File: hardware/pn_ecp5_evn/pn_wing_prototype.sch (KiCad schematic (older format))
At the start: 23 parts, among them J101 Screw_Terminal_01x02, J102 Conn_Coaxial, J103 Conn_02x20_Odd_Even, J104 Conn_Coaxial, J105 Conn_Coaxial, J106 Conn_Coaxial, J107 Conn_01x10

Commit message: added part numbers to schematic of phase noise downconverter, ordered
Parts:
- H101, H102, H103, H104, H105, H106, H107, H108, H109, H110, H111, H112, H113, H114, H115, H116, J107: Distributor Part Number (none) -> N/A
- J101: Distributor (none) -> Digi-Key; Distributor Part Number (none) -> 277-1273-ND
- J102, J104, J105, J106: Distributor (none) -> Digi-Key; Distributor Part Number (none) -> WM5534-ND
- J103: Distributor (none) -> Digi-Key; Distributor Part Number (none) -> S7053-ND
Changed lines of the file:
@@
 F 2 "vna:SMA_Molex_73251-1153_OSHFR408" H 1150 1750 50  0001 C CNN
 F 3 " ~" H 1150 1750 50  0001 C CNN
+F 4 "WM5534-ND" H 1150 1750 50  0001 C CNN "Distributor Part Number"
+F 5 "Digi-Key" H 1150 1750 50  0001 C CNN "Distributor"
 	1    1150 1750
 	-1   0    0    -1
@@
 F 2 "vna:SMA_Molex_73251-1153_OSHFR408" H 9150 1650 50  0001 C CNN
 F 3 " ~" H 9150 1650 50  0001 C CNN
+F 4 "WM5534-ND" H 9150 1650 50  0001 C CNN "Distributor Part Number"
+F 5 "Digi-Key" H 9150 1650 50  0001 C CNN "Distributor"
 	1    9150 1650
 	1    0    0    -1
@@
 F 2 "vna:SMA_Molex_73251-1153_OSHFR408" H 9150 2150 50  0001 C CNN
 F 3 " ~" H 9150 2150 50  0001 C CNN
+F 4 "WM5534-ND" H 9150 2150 50  0001 C CNN "Distributor Part Number"
+F 5 "Digi-Key" H 9150 2150 50  0001 C CNN "Distributor"
 	1    9150 2150
 	1    0    0    -1
@@
 F 2 "vna:SMA_Molex_73251-1153_OSHFR408" H 9150 2700 50  0001 C CNN
 F 3 " ~" H 9150 2700 50  0001 C CNN
+F 4 "WM5534-ND" H 9150 2700 50  0001 C CNN "Distributor Part Number"
+F 5 "Digi-Key" H 9150 2700 50  0001 C CNN "Distributor"
 	1    9150 2700
 	1    0    0    -1
@@
 F 2 "Connector_PinSocket_2.54mm:PinSocket_2x20_P2.54mm_Vertical" H 9050 4850 50  0001 C CNN
 F 3 "~" H 9050 4850 50  0001 C CNN
+F 4 "Digi-Key" H 9050 4850 50  0001 C CNN "Distributor"
+F 5 "S7053-ND " H 9050 4850 50  0001 C CNN "Distributor Part Number"
 	1    9050 4850
 	1    0    0    -1
@@
 F 2 "Connector_PinHeader_2.54mm:PinHeader_1x10_P2.54mm_Vertical" H 10200 4350 50  0001 C CNN
 F 3 "~" H 10200 4350 50  0001 C CNN
+F 4 "N/A" H 10200 4350 50  0001 C CNN "Distributor Part Number"
 	1    10200 4350
 	1    0    0    -1
@@
 F 2 "TerminalBlock_Phoenix:TerminalBlock_Phoenix_MPT-0,5-2-2.54_1x02_P2.54mm_Horizontal" H 1000 5350 50  0001 C CNN
 F 3 "~" H 1000 5350 50  0001 C CNN
+F 4 "Digi-Key" H 1000 5350 50  0001 C CNN "Distributor"
+F 5 "277-1273-ND" H 1000 5350 50  0001 C CNN "Distributor Part Number"
 	1    1000 5350
 	-1   0    0    -1
@@
 F 2 "MountingHole:MountingHole_2.7mm_M2.5_ISO14580_Pad" H 1000 7450 50  0001 C CNN
 F 3 "~" H 1000 7450 50  0001 C CNN
+F 4 "N/A" H 1000 7450 50  0001 C CNN "Distributor Part Number"
 	1    1000 7450
 	1    0    0    -1
@@
 F 2 "MountingHole:MountingHole_2.7mm_M2.5_ISO14580_Pad" H 1300 7450 50  0001 C CNN
 F 3 "~" H 1300 7450 50  0001 C CNN
+F 4 "N/A" H 1300 7450 50  0001 C CNN "Distributor Part Number"
 	1    1300 7450
 	1    0    0    -1
@@
 F 2 "MountingHole:MountingHole_2.7mm_M2.5_ISO14580_Pad" H 1600 7450 50  0001 C CNN
 F 3 "~" H 1600 7450 50  0001 C CNN
+F 4 "N/A" H 1600 7450 50  0001 C CNN "Distributor Part Number"
 	1    1600 7450
 	1    0    0    -1
@@
 F 2 "MountingHole:MountingHole_2.7mm_M2.5_ISO14580_Pad" H 1900 7450 50  0001 C CNN
 F 3 "~" H 1900 7450 50  0001 C CNN
+F 4 "N/A" H 1900 7450 50  0001 C CNN "Distributor Part Number"
 	1    1900 7450
 	1    0    0    -1
@@
 F 2 "MountingHole:MountingHole_2.7mm_M2.5_ISO14580_Pad" H 2200 7450 50  0001 C CNN
 F 3 "~" H 2200 7450 50  0001 C CNN
+F 4 "N/A" H 2200 7450 50  0001 C CNN "Distributor Part Number"
 	1    2200 7450
 	1    0    0    -1
@@
 F 2 "MountingHole:MountingHole_2.7mm_M2.5_ISO14580_Pad" H 2500 7450 50  0001 C CNN
 F 3 "~" H 2500 7450 50  0001 C CNN
+F 4 "N/A" H 2500 7450 50  0001 C CNN "Distributor Part Number"
 	1    2500 7450
 	1    0    0    -1
@@
 F 2 "MountingHole:MountingHole_2.7mm_M2.5_ISO14580_Pad" H 2800 7450 50  0001 C CNN
 F 3 "~" H 2800 7450 50  0001 C CNN
+F 4 "N/A" H 2800 7450 50  0001 C CNN "Distributor Part Number"
 	1    2800 7450
 	1    0    0    -1
@@
 F 2 "MountingHole:MountingHole_2.7mm_M2.5_ISO14580_Pad" H 3100 7450 50  0001 C CNN
 F 3 "~" H 3100 7450 50  0001 C CNN
+F 4 "N/A" H 3100 7450 50  0001 C CNN "Distributor Part Number"
 	1    3100 7450
 	1    0    0    -1
@@
 F 2 "MountingHole:MountingHole_2.7mm_M2.5_ISO14580_Pad" H 3400 7450 50  0001 C CNN
 F 3 "~" H 3400 7450 50  0001 C CNN
+F 4 "N/A" H 3400 7450 50  0001 C CNN "Distributor Part Number"
 	1    3400 7450
 	1    0    0    -1
@@
 F 2 "MountingHole:MountingHole_2.7mm_M2.5_ISO14580_Pad" H 3700 7450 50  0001 C CNN
 F 3 "~" H 3700 7450 50  0001 C CNN
+F 4 "N/A" H 3700 7450 50  0001 C CNN "Distributor Part Number"
 	1    3700 7450
 	1    0    0    -1
@@
 F 2 "MountingHole:MountingHole_2.7mm_M2.5_ISO14580_Pad" H 4000 7450 50  0001 C CNN
 F 3 "~" H 4000 7450 50  0001 C CNN
+F 4 "N/A" H 4000 7450 50  0001 C CNN "Distributor Part Number"
 	1    4000 7450
 	1    0    0    -1
@@
 F 2 "MountingHole:MountingHole_2.7mm_M2.5_ISO14580_Pad" H 4300 7450 50  0001 C CNN
 F 3 "~" H 4300 7450 50  0001 C CNN
+F 4 "N/A" H 4300 7450 50  0001 C CNN "Distributor Part Number"
 	1    4300 7450
 	1    0    0    -1
@@
 F 2 "MountingHole:MountingHole_2.7mm_M2.5_ISO14580_Pad" H 4650 7450 50  0001 C CNN
 F 3 "~" H 4650 7450 50  0001 C CNN
+F 4 "N/A" H 4650 7450 50  0001 C CNN "Distributor Part Number"
 	1    4650 7450
 	1    0    0    -1
@@
 F 2 "MountingHole:MountingHole_2.7mm_M2.5_ISO14580_Pad" H 4950 7450 50  0001 C CNN
 F 3 "~" H 4950 7450 50  0001 C CNN
+F 4 "N/A" H 4950 7450 50  0001 C CNN "Distributor Part Number"
 	1    4950 7450
 	1    0    0    -1
@@
 F 2 "MountingHole:MountingHole_2.7mm_M2.5_ISO14580_Pad" H 5400 7450 50  0001 C CNN
 F 3 "~" H 5400 7450 50  0001 C CNN
+F 4 "N/A" H 5400 7450 50  0001 C CNN "Distributor Part Number"
 	1    5400 7450
 	1    0    0    -1
@@
 F 2 "MountingHole:MountingHole_2.7mm_M2.5_ISO14580_Pad" H 5800 7450 50  0001 C CNN
 F 3 "~" H 5800 7450 50  0001 C CNN
+F 4 "N/A" H 5800 7450 50  0001 C CNN "Distributor Part Number"
 	1    5800 7450
 	1    0    0    -1

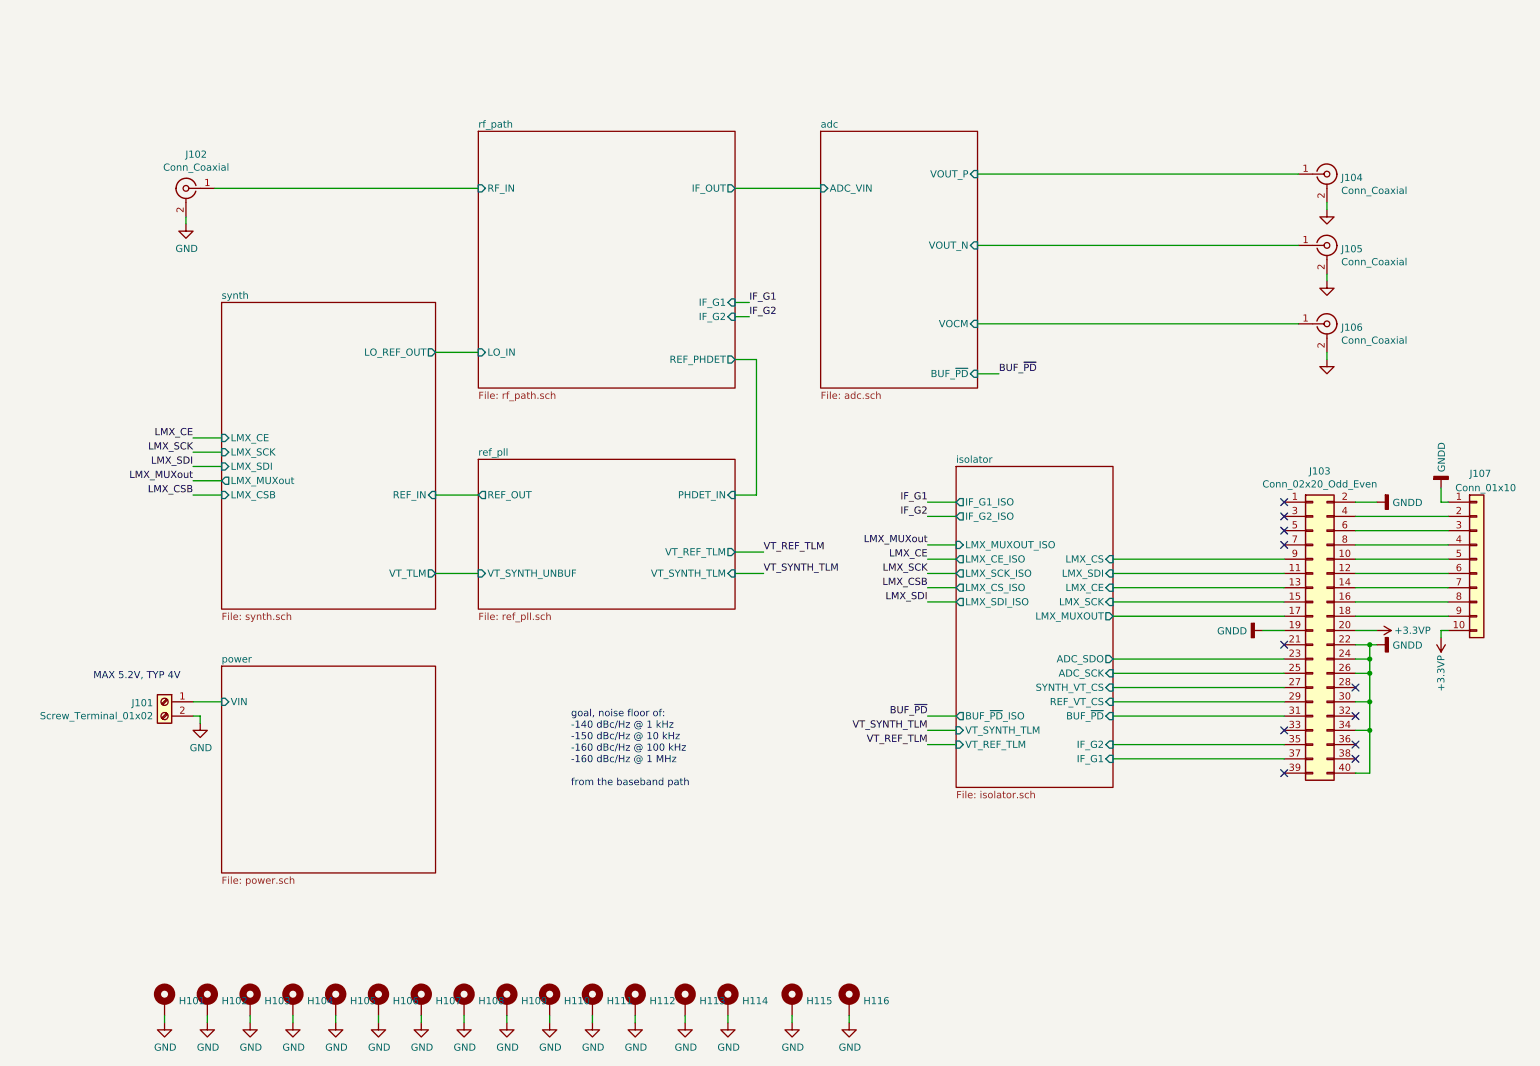
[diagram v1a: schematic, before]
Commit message: added schematic export, updated README, schematic cleanup
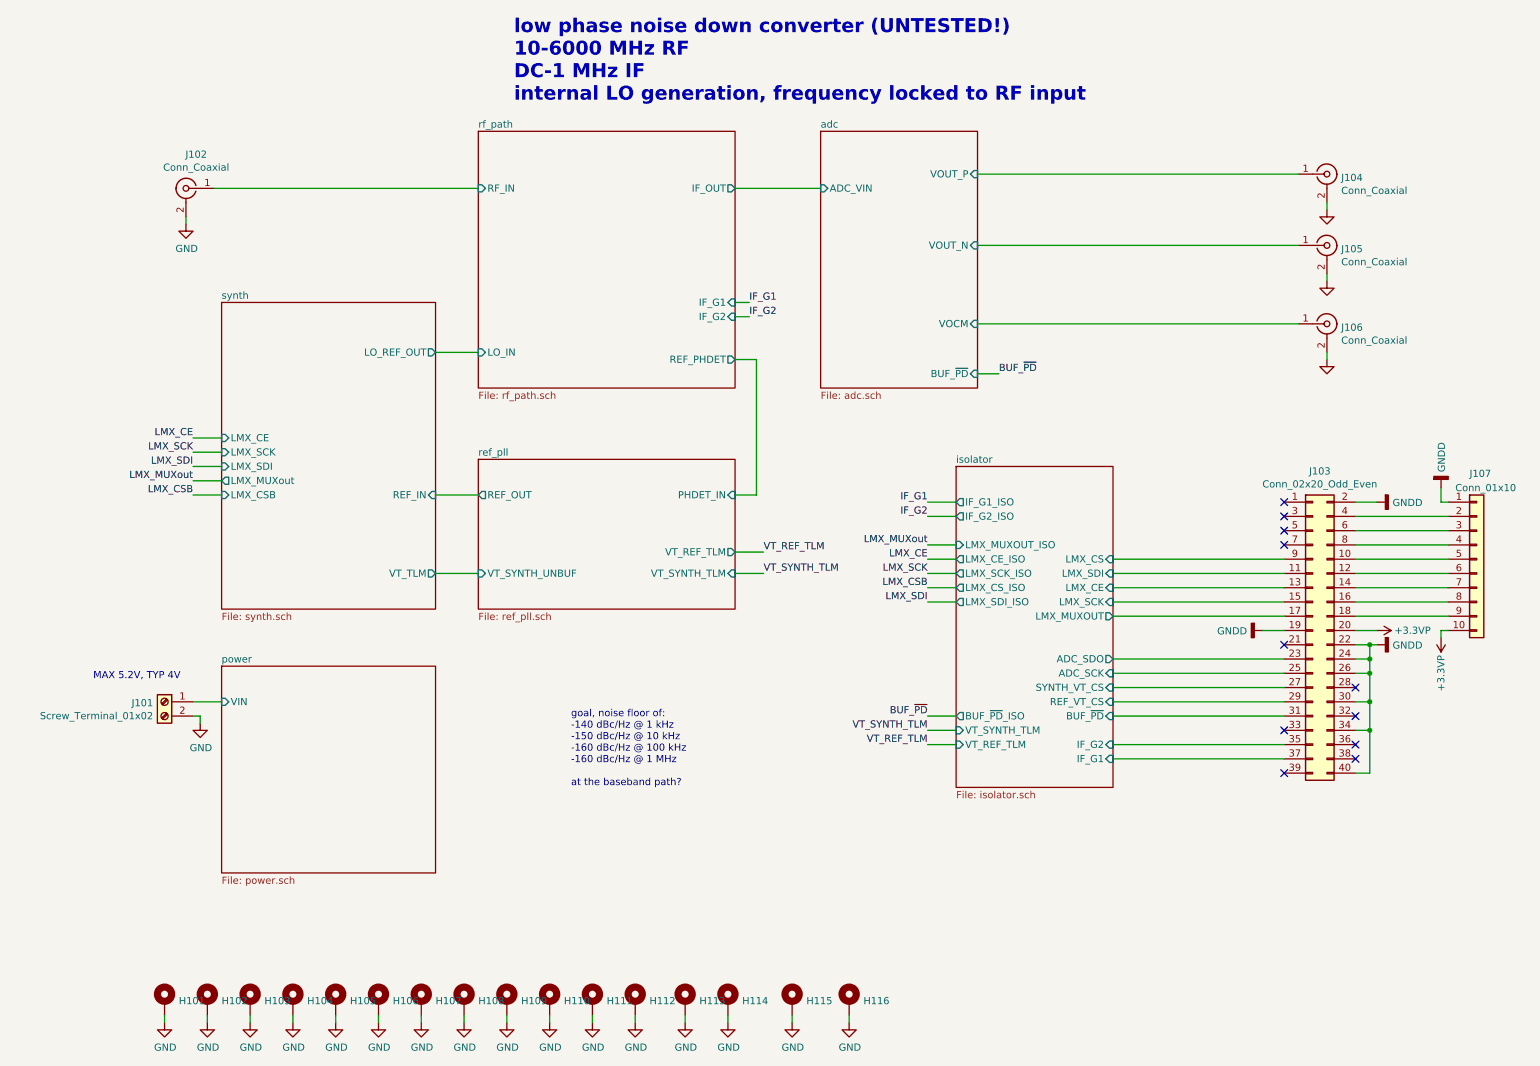
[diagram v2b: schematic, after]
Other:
- note added: "goal, noise floor of:\n-140 dBc/Hz @ 1 kHz\n-150 dBc/Hz @ 10 kHz\n-160 dBc/Hz @ 100 kHz\n-160 dBc/Hz @ 1 MHz\n\nat the baseband path?"
- note added: "low phase noise down converter (UNTESTED!)\n10-6000 MHz RF\nDC-1 MHz IF\ninternal LO generation, frequency locked to RF input"
- note removed: "goal, noise floor of:\n-140 dBc/Hz @ 1 kHz\n-150 dBc/Hz @ 10 kHz\n-160 dBc/Hz @ 100 kHz\n-160 dBc/Hz @ 1 MHz\n\nfrom the baseband path"
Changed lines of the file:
@@
 IF_G2
 Text Notes 3850 5950 0    50   ~ 0
-goal, noise floor of:\n-140 dBc/Hz @ 1 kHz\n-150 dBc/Hz @ 10 kHz\n-160 dBc/Hz @ 100 kHz\n-160 dBc/Hz @ 1 MHz\n\nfrom the baseband path
+goal, noise floor of:\n-140 dBc/Hz @ 1 kHz\n-150 dBc/Hz @ 10 kHz\n-160 dBc/Hz @ 100 kHz\n-160 dBc/Hz @ 1 MHz\n\nat the baseband path?
 Wire Wire Line
 	5100 2550 5000 2550
@@
 Wire Wire Line
 	7650 5750 8850 5750
+Text Notes 3450 1150 0    98   ~ 20
+low phase noise down converter (UNTESTED!)\n10-6000 MHz RF\nDC-1 MHz IF\ninternal LO generation, frequency locked to RF input
 $EndSCHEMATC

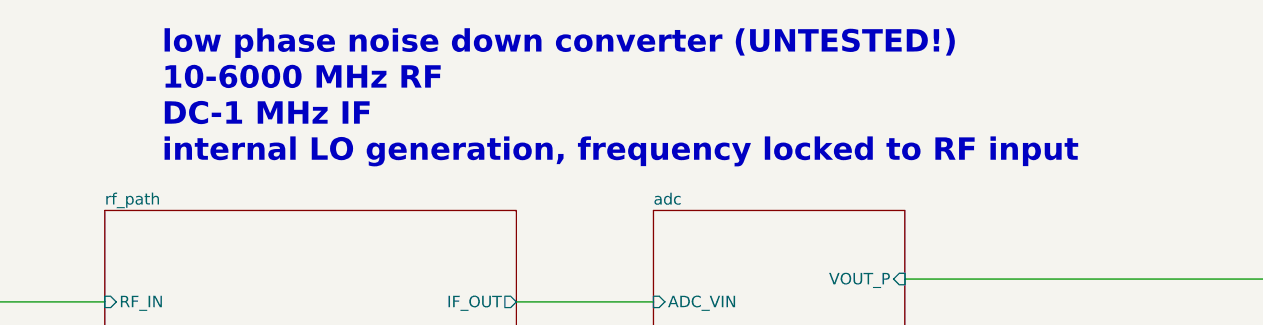
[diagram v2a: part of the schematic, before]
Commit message: updated schematic export with pll fix
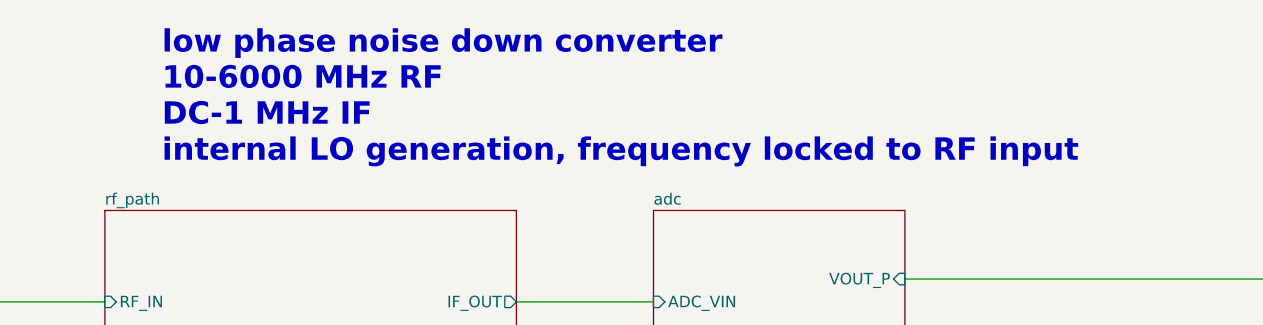
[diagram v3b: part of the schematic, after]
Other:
- note added: "low phase noise down converter\n10-6000 MHz RF\nDC-1 MHz IF\ninternal LO generation, frequency locked to RF input"
- note removed: "low phase noise down converter (UNTESTED!)\n10-6000 MHz RF\nDC-1 MHz IF\ninternal LO generation, frequency locked to RF input"
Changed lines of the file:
@@
 	7650 5750 8850 5750
 Text Notes 3450 1150 0    98   ~ 20
-low phase noise down converter (UNTESTED!)\n10-6000 MHz RF\nDC-1 MHz IF\ninternal LO generation, frequency locked to RF input
+low phase noise down converter\n10-6000 MHz RF\nDC-1 MHz IF\ninternal LO generation, frequency locked to RF input
 $EndSCHEMATC
